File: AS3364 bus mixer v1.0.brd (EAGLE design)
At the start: 41.3 x 16.2 mm, 63 parts, among them IC1 TL072JD, IC2 TL072JD, IC3 TL072JD, IC30 TL072JT, IC4 TL072JD, IC5 79L09F, IC6 78L09F, IC7 CH446Q

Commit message: Tracing the bus mixer
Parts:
- removed SV1: (no value), joakim:SIP-PIN15-1J
- added +12V, -12V, BC_IN, BUS_A, BUS_B, CS/CK, CV1, CV2, CV3, CV4, CV5, CV6, CV7, CV8, DAT, DIST_IN, FX_A, FX_B, GND, IN1, IN2, IN3, IN4, IN5, IN6, IN7, IN8, RST, STB: (no value), joakim:MA01NS-1J
- IC1, IC2, IC3, IC4: value TL072JD -> TL072JT; device joakim:SO08J -> joakim:TSSOP8J
- R14, R15, R16, R17, R31, R32, R33, R34, R47, R48: device rcl:R0603 -> rcl:R0402
- moved C15 172.5 mm to (69.2, 19.1)
- moved C14 165.4 mm to (64.5, 18.7)
- moved C13 161.5 mm to (75.9, 27.0)
- moved C8 161.5 mm to (75.9, 21.9)
- moved IC7 156.2 mm to (17.5, 23.8)
- moved IC5 155.5 mm to (39.4, 27.6)
- moved IC6 146.0 mm to (38.7, 20.6)
- moved C4 128.1 mm to (56.5, 24.8), turned to 90 degrees
- moved C7 119.5 mm to (40.6, 12.1), turned to 180 degrees
- moved C3 113.1 mm to (28.3, 24.4), turned to 90 degrees
- moved C6 109.9 mm to (23.5, 12.1)
- moved C2 107.1 mm to (22.2, 24.8), turned to 90 degrees
- moved R23 92.8 mm to (30.2, 17.8), turned to 90 degrees
- moved R31 92.6 mm to (25.8, 30.6), turned to 90 degrees
- moved R32 92.0 mm to (27.7, 30.6), turned to 90 degrees
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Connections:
- new net BITCRUSH_IN: BC_IN.1, IC7.15
- new net CS/CK: CS/CK.1, IC7.34
- new net CV5: CV5.1, R19.1
- new net CV6: CV6.1, R20.1
- new net CV6_IN: DA1.3, R20.2, R28.2
- new net CV7: CV7.1, R18.1
- new net CV8: CV8.1, R21.1
- new net DAT: DAT.1, IC7.36
- new net DIST_IN: DIST_IN.1, IC7.17
- new net FX_A: FX_A.1, IC7.37
- new net FX_B: FX_B.1, IC7.39
- new net IN5: DA1.15, IN5.1
- new net IN6: DA1.2, IN6.1
- new net IN7: DA1.10, IN7.1
- new net IN8: DA1.7, IN8.1
- new net OUT5: IC4.1, IC4.2, R34.1
- new net OUT6: IC4.6, IC4.7, R31.1
- new net OUT7: IC3.1, IC3.2, R33.1
- new net OUT8: IC3.6, IC3.7, R32.1
- new net RST: IC7.41, RST.1
- new net STB: IC7.14, STB.1
- new net SW1: IC7.31, R17.2
- new net SW2: IC7.30, R14.2
- new net SW3: IC7.29, R16.2
- new net SW4: IC7.28, R15.2
- new net SW5: IC7.27, R34.2
- new net SW6: IC7.26, R31.2
- new net SW7: IC7.3, R33.2
- new net SW8: IC7.4, R32.2
- net +12V: now also +12V.1; no longer SV1.14
- net -12V: now also -12V.1; no longer SV1.13
- net BUS_A: now also BUS_A.1, IC7.33
- net BUS_B: now also BUS_B.1, IC7.35
- net CV1: now also CV1.1; no longer R19.1, SV1.5
- net CV2: now also CV2.1; no longer R20.1, SV1.6
- net CV2_IN: no longer DA1.3, R20.2, R28.2
- net CV3: now also CV3.1; no longer R18.1, SV1.7
- net CV4: now also CV4.1; no longer R21.1, SV1.8
- net GND: now also GND.1; no longer SV1.15
- net IN1: now also IN1.1; no longer DA1.15, SV1.3
- net IN2: now also IN2.1; no longer DA1.2, SV1.4
- net IN3: now also IN3.1; no longer DA1.10, SV1.9
- net IN4: now also IN4.1; no longer DA1.7, SV1.10
- net OUT1: no longer IC4.1, IC4.2, R34.1, SV1.1
- net OUT2: no longer IC4.6, IC4.7, R31.1, SV1.2
- net OUT3: no longer IC3.1, IC3.2, R33.1, SV1.11
- net OUT4: no longer IC3.6, IC3.7, R32.1, SV1.12
- net SUM_A: now also IC30.7, IC7.5, R47.2; no longer IC30.1, R48.2
- net SUM_B: now also IC30.1, IC7.6, R48.2; no longer IC30.7, R47.2
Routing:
- net -12V: track 63.7 -> 42.7 mm, vias 4 -> 2
- net OUT3: track 20.9 -> 0.00 mm, vias 1 -> 0
- net GND: track 104.5 -> 84.7 mm
- net N$13: track 20.6 -> 2.69 mm
- net N$11: track 20.3 -> 2.69 mm
- net IN7: track 0.00 -> 16.5 mm
- net OUT1: track 16.4 -> 0.00 mm, vias 1 -> 0
- net CV7: track 0.00 -> 15.5 mm, vias 0 -> 1
- net STB: track 0.00 -> 14.4 mm
- net DAT: track 0.00 -> 14.4 mm
- net OUT4: track 13.1 -> 0.00 mm, vias 1 -> 0
- net CV5: track 0.00 -> 12.9 mm, vias 0 -> 1
- net CV8: track 0.00 -> 11.5 mm, vias 0 -> 1
- net RST: track 0.00 -> 10.9 mm
- net IN5: track 0.00 -> 10.9 mm
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- removed copper zone on layer 16, net GND
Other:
- board size 41.3 x 16.2 mm -> 78.1 x 31.1 mm

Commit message: Most of lower part traced ok
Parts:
- added STB1, STB2, STB3: (no value), joakim:MA01NS-1J
- moved BC_IN 15.2 mm to (25.4, 1.27)
- moved DIST_IN 15.2 mm to (25.4, 3.81)
- moved BUS_B 5.08 mm to (40.6, 1.27)
- moved CV5 2.54 mm to (27.9, 1.27)
- moved IN5 2.54 mm to (27.9, 3.81)
- moved IN7 2.54 mm to (33.0, 3.81)
- moved -12V 2.54 mm to (22.9, 3.81)
- moved CS/CK 2.54 mm to (2.54, 3.81)
- moved RST 2.54 mm to (5.08, 3.81)
- moved CV6 2.54 mm to (30.5, 1.27)
- moved CV7 2.54 mm to (33.3, 1.27)
- moved CV8 2.54 mm to (35.6, 1.27)
- moved FX_A 2.54 mm to (38.1, 3.81)
- moved FX_B 2.54 mm to (40.6, 3.81)
- moved IN6 2.54 mm to (30.5, 3.81)
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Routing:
- net BITCRUSH_IN: track 0.00 -> 16.3 mm
- net BUS_A: track 0.00 -> 16.3 mm
- net BUS_B: track 0.00 -> 14.4 mm
- net FX_A: track 0.00 -> 13.4 mm
- net FX_B: track 0.00 -> 12.2 mm
- net DIST_IN: track 0.00 -> 11.7 mm
- net N$15: track 0.00 -> 10.6 mm
- net N$9: track 0.00 -> 10.1 mm
- net CS/CK: track 1.98 -> 11.6 mm
- net CV2: track 16.0 -> 10.7 mm
- net N$6: track 10.6 -> 14.6 mm
- net IN7: track 16.5 -> 12.5 mm
- net +12V: track 41.3 -> 45.2 mm
- net RST: track 10.9 -> 14.4 mm
- net CV6: track 9.65 -> 12.9 mm
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
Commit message: Missing 12V to left side only
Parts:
- removed C14, C8: 0.1uF, resistor:C0603
- added C16, C17: 100nF, rcl:C0402
- moved C13 45.4 mm to (30.5, 27.9), turned to 270 degrees
- moved C15 38.7 mm to (30.5, 18.7), turned to 270 degrees
- moved C4 26.1 mm to (30.5, 23.2)
- moved R48 19.5 mm to (40.6, 18.1)
- moved C2 17.2 mm to (39.4, 23.2)
- moved R25 16.0 mm to (38.1, 27.9), turned to 270 degrees
- moved IC5 14.9 mm to (27.0, 19.4), turned to 180 degrees
- moved R16 14.1 mm to (0.32, 18.4), turned to 270 degrees
- moved IC6 13.2 mm to (27.0, 26.7)
- moved R47 12.8 mm to (41.9, 27.9)
- moved R17 12.6 mm to (4.76, 18.4), turned to 270 degrees
- moved R34 12.5 mm to (36.2, 18.4), turned to 270 degrees
- moved R24 12.1 mm to (33.7, 27.9), turned to 270 degrees
- moved R33 12.1 mm to (32.1, 18.4), turned to 270 degrees
- moved R31 11.4 mm to (36.8, 27.9)
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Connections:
- removed net AGND: IC30.3, IC30.5
- removed net N$11: DA2.12, IC1.3, R6.2
- removed net N$13: DA2.13, IC2.3, R5.2
- removed net N$15: DA1.5, IC3.5, R24.2
- removed net N$16: DA1.12, IC3.3, R23.2
- removed net N$17: DA1.13, IC4.3, R22.2
- removed net N$4: DA2.4, IC2.5, R8.2
- removed net N$6: DA2.5, IC1.5, R7.2
- removed net N$9: DA1.4, IC4.5, R25.2
- new net CON1: DA2.13, IC1.3, R6.2
- new net CON2: DA2.4, IC1.5, R7.2
- new net CON3: DA2.12, IC2.3, R5.2
- new net CON4: DA2.5, IC2.5, R8.2
- new net CON5: DA1.13, IC3.3, R23.2
- new net CON6: DA1.4, IC3.5, R24.2
- new net CON7: DA1.12, IC4.3, R22.2
- new net CON8: DA1.5, IC4.5, R25.2
- net +9V: now also C17.1; no longer C8.2
- net -9V: now also C16.2; no longer C14.1
- net BUS_A: now also IC7.13; no longer IC7.33
- net BUS_B: now also IC7.11; no longer IC7.35
- net FX_A: now also IC7.39; no longer IC7.37
- net FX_B: now also IC7.37; no longer IC7.39
- net GND: now also C16.1, C17.2, IC30.3, IC30.5; no longer C14.2, C8.1
- net SW1: now also IC7.29, R16.2; no longer IC7.31, R17.2
- net SW2: now also IC7.28, R15.2; no longer IC7.30, R14.2
- net SW3: now also IC7.31, R17.2; no longer IC7.29, R16.2
- net SW4: now also IC7.30, R14.2; no longer IC7.28, R15.2
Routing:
- net GND: track 85.3 -> 236.4 mm, vias 12 -> 17
- net +12V: track 45.2 -> 110.1 mm, vias 1 -> 3
- net -12V: track 41.2 -> 99.3 mm, vias 2 -> 4
- net BUS_A: track 16.3 -> 61.6 mm, vias 0 -> 2
- net FX_B: track 12.2 -> 53.0 mm, vias 0 -> 1
- net BUS_B: track 14.4 -> 54.9 mm, vias 0 -> 6
- net FX_A: track 13.4 -> 51.0 mm, vias 0 -> 1
- net SUM_A: track 0.00 -> 37.5 mm, vias 0 -> 2
- net SUM_B: track 0.00 -> 34.0 mm, vias 0 -> 4
- net SW1: track 0.00 -> 28.0 mm, vias 0 -> 2
- net SW5: track 0.00 -> 26.4 mm, vias 0 -> 2
- net SW8: track 0.00 -> 26.3 mm, vias 0 -> 2
- net +9V: track 0.00 -> 26.3 mm, vias 0 -> 2
- net CON2: track 0.00 -> 25.9 mm, vias 0 -> 1
- net STB: track 17.2 -> 42.1 mm, vias 0 -> 2
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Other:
- board size 78.1 x 31.1 mm -> 44.4 x 31.1 mm

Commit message: all traced
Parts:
- moved C2 0.64 mm to (40.0, 23.2)
- moved C3 0.64 mm to (35.6, 23.2)
- moved DA1 0.64 mm to (33.0, 10.2)
- moved R26 0.64 mm to (34.6, 12.1)
- moved R29 0.64 mm to (34.6, 8.26)
- moved R31 0.64 mm to (37.5, 27.9)
- moved R32 0.64 mm to (33.0, 27.9)
- moved R47 0.64 mm to (42.5, 27.9)
- moved -12V 0.64 mm to (23.5, 3.81)
- moved BC_IN 0.64 mm to (26.0, 3.81)
- moved C1 0.64 mm to (20.0, 8.26)
- moved C16 0.64 mm to (24.4, 23.2)
- moved C6 0.64 mm to (24.4, 12.1)
- moved C9 0.64 mm to (20.0, 12.1)
- moved CV2 0.64 mm to (13.3, 1.27)
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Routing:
- net +12V: track 110.1 -> 128.9 mm, vias 3 -> 5
- net GND: track 236.4 -> 235.9 mm
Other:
- board size 44.4 x 31.1 mm -> 44.5 x 30.5 mm

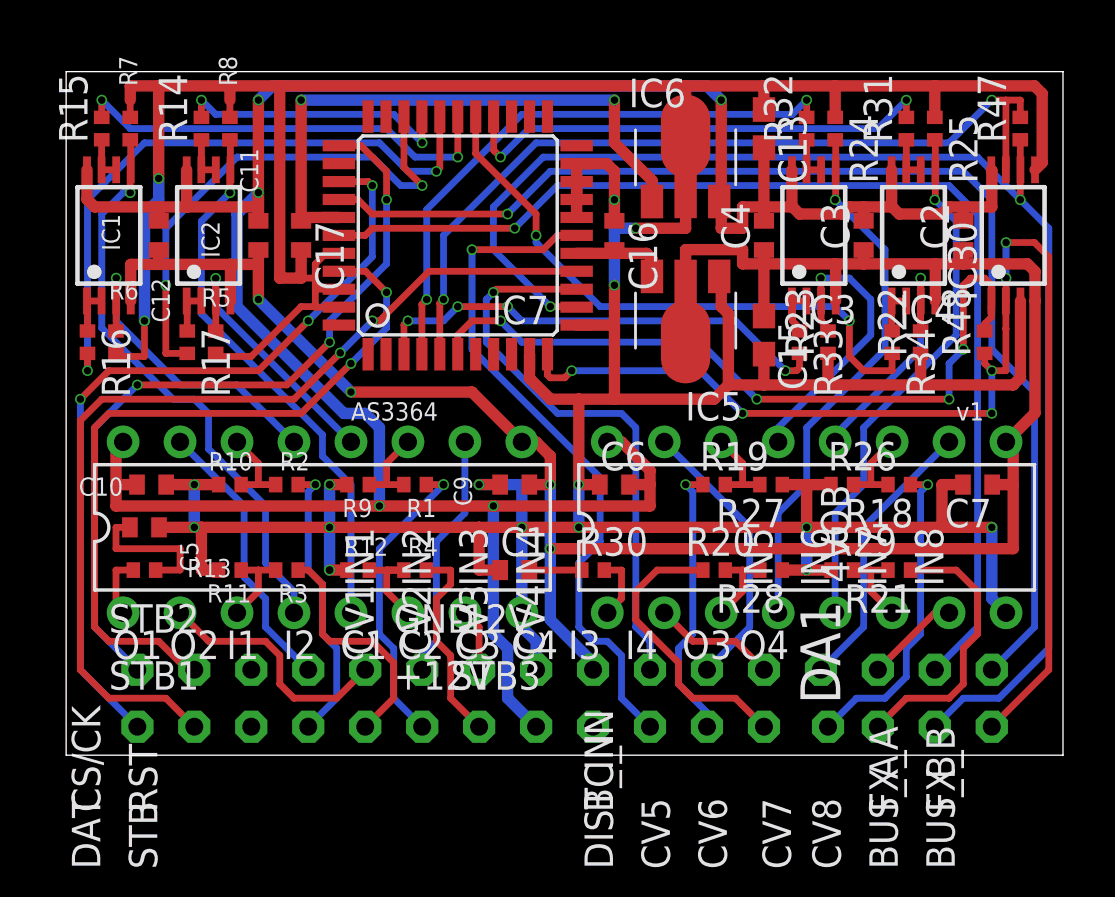
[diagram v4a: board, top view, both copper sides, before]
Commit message: Reordered lines to make coding easier
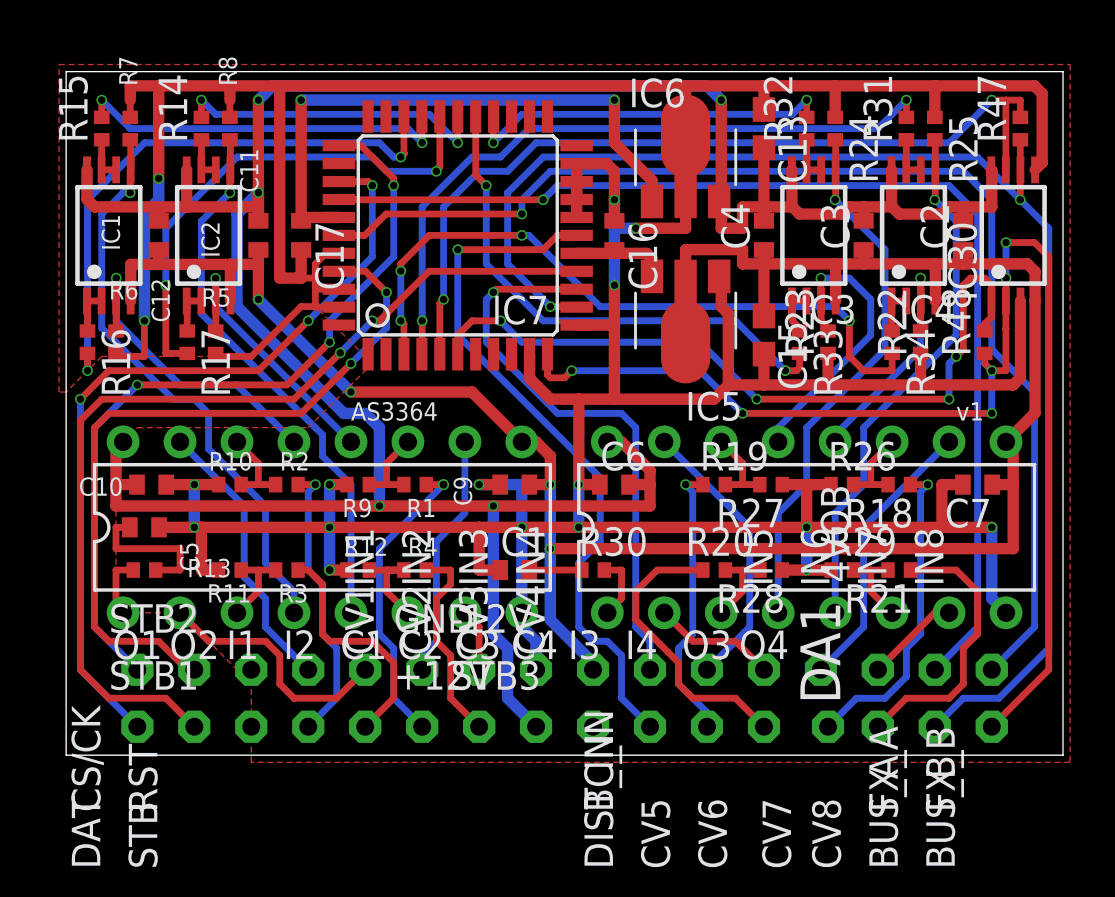
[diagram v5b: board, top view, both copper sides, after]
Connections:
- net FX_A: now also IC7.37; no longer IC7.39
- net FX_B: now also IC7.39; no longer IC7.37
- net OUT1: now also IC1.1, IC1.2, R16.1; no longer IC2.1, IC2.2, R17.1
- net OUT2: now also IC1.6, IC1.7, R15.1; no longer IC2.6, IC2.7, R14.1
- net OUT3: now also IC2.1, IC2.2, R17.1; no longer IC1.1, IC1.2, R16.1
- net OUT4: now also IC2.6, IC2.7, R14.1; no longer IC1.6, IC1.7, R15.1
- net OUT5: now also IC3.1, IC3.2, R33.1; no longer IC4.1, IC4.2, R34.1
- net OUT6: now also IC3.6, IC3.7, R32.1; no longer IC4.6, IC4.7, R31.1
- net OUT7: now also IC4.1, IC4.2, R34.1; no longer IC3.1, IC3.2, R33.1
- net OUT8: now also IC4.6, IC4.7, R31.1; no longer IC3.6, IC3.7, R32.1
- net SW1: now also IC7.31; no longer IC7.29
- net SW2: now also IC7.30; no longer IC7.28
- net SW3: now also IC7.29; no longer IC7.31
- net SW4: now also IC7.28; no longer IC7.30
- net SW5: now also R33.2; no longer R34.2
- net SW6: now also R32.2; no longer R31.2
- net SW7: now also R34.2; no longer R33.2
- net SW8: now also R31.2; no longer R32.2
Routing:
- net SW7: track 21.2 -> 30.7 mm
- net SW6: track 21.9 -> 16.7 mm
- net SW8: track 26.3 -> 30.9 mm
- net SW5: track 26.7 -> 23.4 mm
- net SW1: track 28.0 -> 25.6 mm
- net SW2: track 19.5 -> 17.0 mm
- net SW4: track 12.6 -> 14.2 mm
- net DIST_IN: track 30.6 -> 31.5 mm
- net SUM_A: track 37.5 -> 38.2 mm
- net FX_A: track 51.0 -> 50.4 mm
- net SW3: track 23.2 -> 22.7 mm
- net BUS_A: track 61.6 -> 61.1 mm
- added copper zone on layer 1, net GND

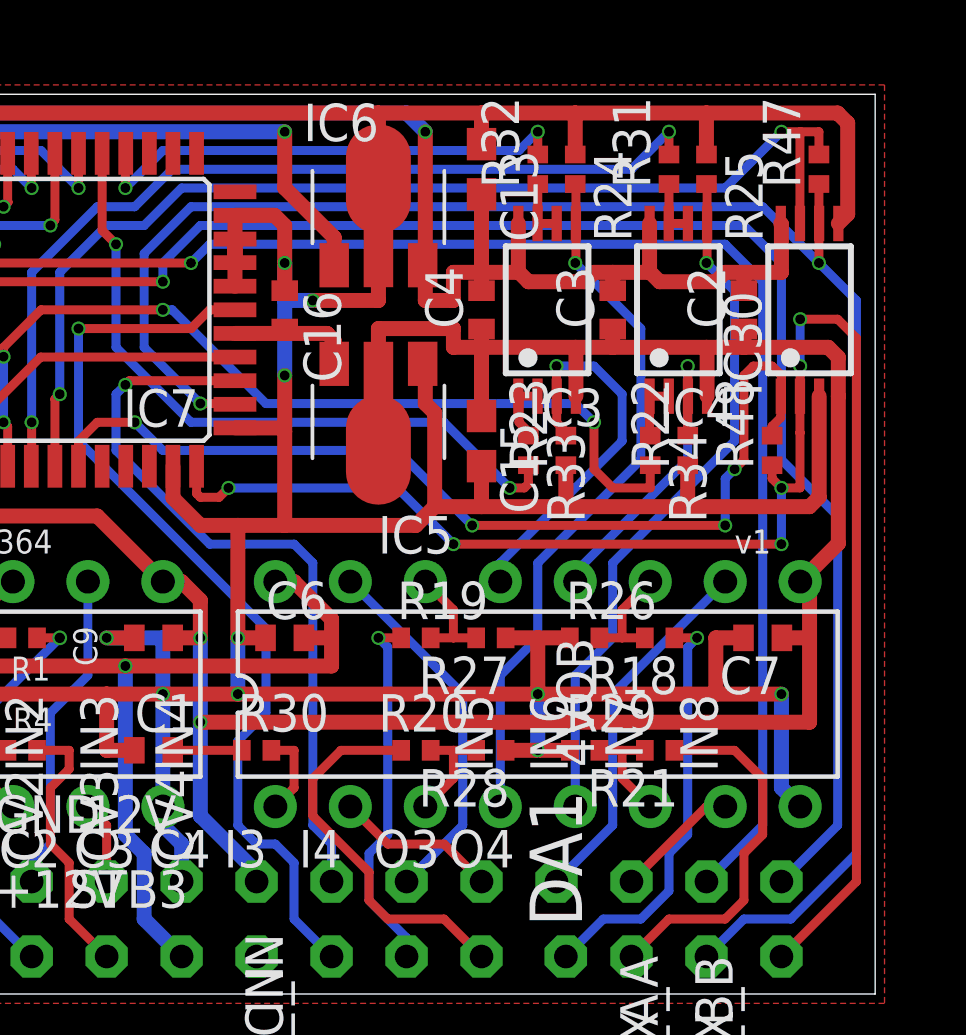
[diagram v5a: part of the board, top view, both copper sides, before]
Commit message: Added 220k resistors to bus
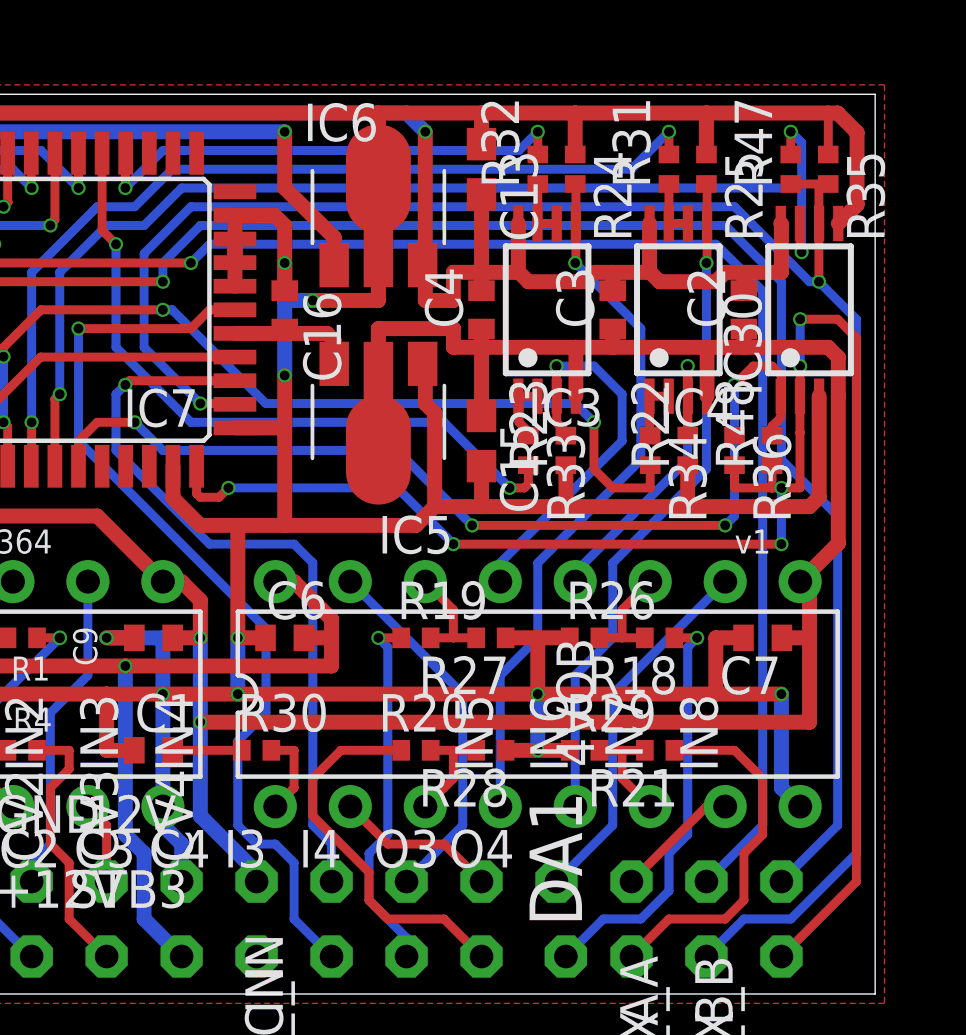
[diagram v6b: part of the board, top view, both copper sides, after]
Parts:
- added R35, R36: 220k, rcl:R0402
- moved R47 0.95 mm to (41.6, 27.9)
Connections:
- net BUS_A: now also R35.2
- net BUS_B: now also R36.2
- net GND: now also R35.1, R36.1
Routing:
- net BUS_B: track 55.0 -> 57.3 mm
- net GND: track 235.9 -> 237.5 mm
- net BUS_A: track 61.1 -> 62.6 mm
- net SUM_A: track 38.2 -> 39.0 mm, vias 2 -> 3
- net CON8: track 23.7 -> 22.9 mm
